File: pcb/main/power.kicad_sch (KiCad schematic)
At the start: 13 parts, among them U1 LXDC55FAAA-203, U2 LT1963AES3-3.3

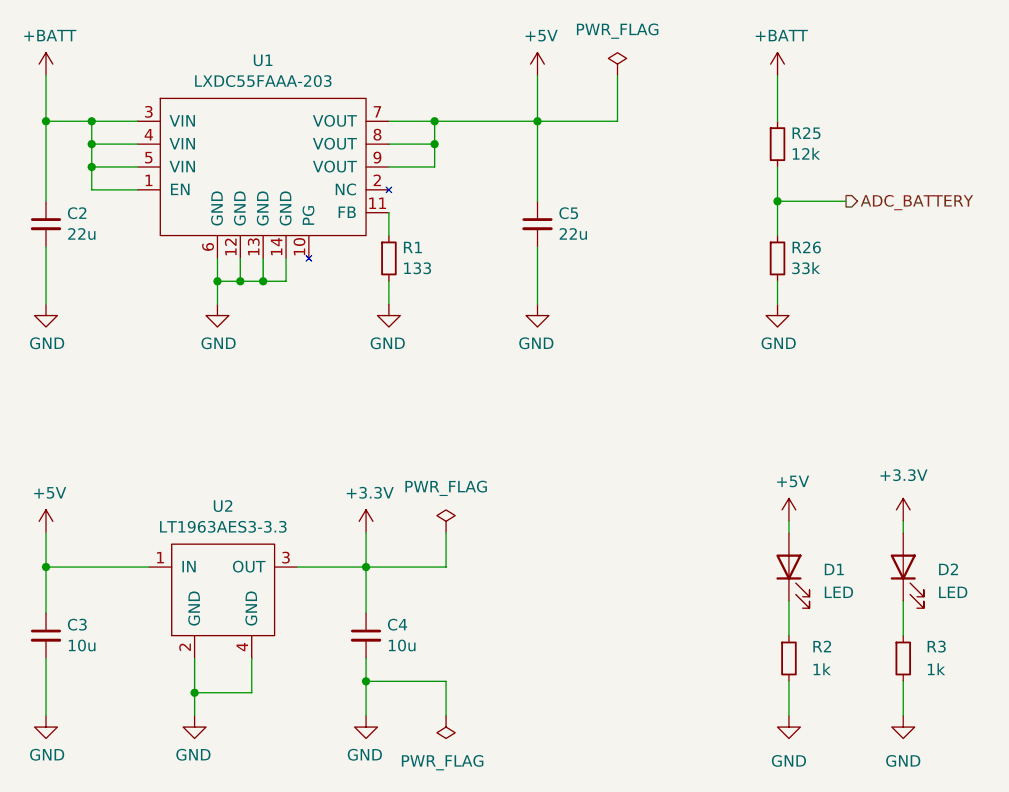
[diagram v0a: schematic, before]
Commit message: feat: delete two CAN connectors & add microSD input pin
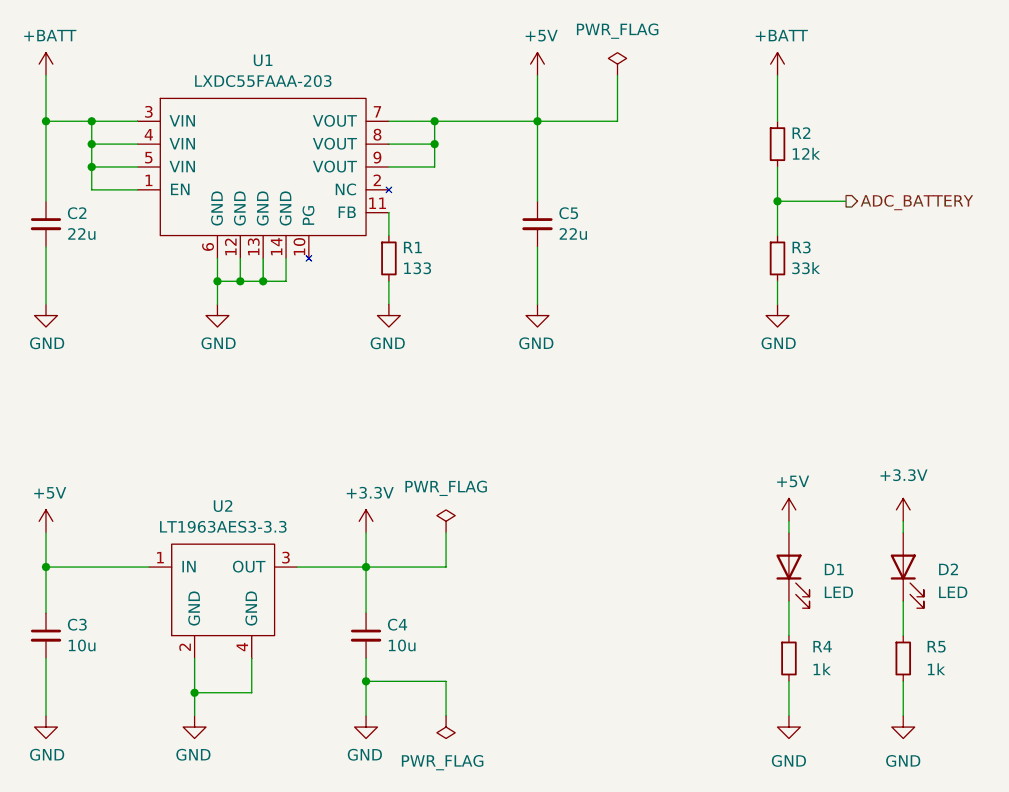
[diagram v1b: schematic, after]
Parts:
- renumbered R25 to R2, R26 to R3, R2 to R4, R3 to R5
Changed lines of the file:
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@@
 		(on_board yes)
 		(dnp no)
-		(property "Reference" "#PWR034"
+		(property "Reference" "#PWR032"
 			(at 184.15 104.14 0)
 			(effects
@@
 			(project "main"
 				(path "/656d7f7e-2105-4d24-8d0a-93f423922a26/b1cff48c-95d9-4c57-9a68-4399c567f645"
-					(reference "#PWR034")
+					(reference "#PWR032")
 					(unit 1)
 				)
@@
 		(on_board yes)
 		(dnp no)
-		(property "Reference" "#PWR024"
+		(property "Reference" "#PWR020"
 			(at 101.6 82.55 0)
 			(effects
@@
 			(project ""
 				(path "/656d7f7e-2105-4d24-8d0a-93f423922a26/b1cff48c-95d9-4c57-9a68-4399c567f645"
-					(reference "#PWR024")
+					(reference "#PWR020")
 					(unit 1)
 				)
@@
 		(on_board yes)
 		(dnp no)
-		(property "Reference" "#PWR025"
+		(property "Reference" "#PWR021"
 			(at 101.6 105.41 0)
 			(effects
@@
 			(project "main"
 				(path "/656d7f7e-2105-4d24-8d0a-93f423922a26/b1cff48c-95d9-4c57-9a68-4399c567f645"
-					(reference "#PWR025")
+					(reference "#PWR021")
 					(unit 1)
 				)
@@
 		(dnp no)
 		(fields_autoplaced yes)
-		(property "Reference" "R2"
+		(property "Reference" "R4"
 			(at 186.69 114.2999 0)
 			(effects
@@
 			(project "main"
 				(path "/656d7f7e-2105-4d24-8d0a-93f423922a26/b1cff48c-95d9-4c57-9a68-4399c567f645"
-					(reference "R2")
+					(reference "R4")
 					(unit 1)
 				)
@@
 		(on_board yes)
 		(dnp no)
-		(property "Reference" "#PWR074"
+		(property "Reference" "#PWR030"
 			(at 182.88 54.61 0)
 			(effects
@@
 			(project "main"
 				(path "/656d7f7e-2105-4d24-8d0a-93f423922a26/b1cff48c-95d9-4c57-9a68-4399c567f645"
-					(reference "#PWR074")
+					(reference "#PWR030")
 					(unit 1)
 				)
@@
 		(dnp no)
 		(fields_autoplaced yes)
-		(property "Reference" "#PWR037"
+		(property "Reference" "#PWR035"
 			(at 196.85 128.27 0)
 			(effects
@@
 			(project ""
 				(path "/656d7f7e-2105-4d24-8d0a-93f423922a26/b1cff48c-95d9-4c57-9a68-4399c567f645"
-					(reference "#PWR037")
+					(reference "#PWR035")
 					(unit 1)
 				)
@@
 		(on_board yes)
 		(dnp no)
-		(property "Reference" "R25"
+		(property "Reference" "R2"
 			(at 184.3786 57.2516 0)
 			(effects
@@
 			(project "main"
 				(path "/656d7f7e-2105-4d24-8d0a-93f423922a26/b1cff48c-95d9-4c57-9a68-4399c567f645"
-					(reference "R25")
+					(reference "R2")
 					(unit 1)
 				)
@@
 		(on_board yes)
 		(dnp no)
-		(property "Reference" "#PWR026"
+		(property "Reference" "#PWR022"
 			(at 101.6 128.27 0)
 			(effects
@@
 			(project "main"
 				(path "/656d7f7e-2105-4d24-8d0a-93f423922a26/b1cff48c-95d9-4c57-9a68-4399c567f645"
-					(reference "#PWR026")
+					(reference "#PWR022")
 					(unit 1)
 				)
@@
 		(dnp no)
 		(fields_autoplaced yes)
-		(property "Reference" "#PWR035"
+		(property "Reference" "#PWR033"
 			(at 184.15 128.27 0)
 			(effects
@@
 			(project "main"
 				(path "/656d7f7e-2105-4d24-8d0a-93f423922a26/b1cff48c-95d9-4c57-9a68-4399c567f645"
-					(reference "#PWR035")
+					(reference "#PWR033")
 					(unit 1)
 				)
@@
 		(on_board yes)
 		(dnp no)
-		(property "Reference" "#PWR073"
+		(property "Reference" "#PWR031"
 			(at 182.88 82.55 0)
 			(effects
@@
 			(project "main"
 				(path "/656d7f7e-2105-4d24-8d0a-93f423922a26/b1cff48c-95d9-4c57-9a68-4399c567f645"
-					(reference "#PWR073")
+					(reference "#PWR031")
 					(unit 1)
 				)
@@
 		(on_board yes)
 		(dnp no)
-		(property "Reference" "#PWR028"
+		(property "Reference" "#PWR024"
 			(at 120.65 82.55 0)
 			(effects
@@
 			(project ""
 				(path "/656d7f7e-2105-4d24-8d0a-93f423922a26/b1cff48c-95d9-4c57-9a68-4399c567f645"
-					(reference "#PWR028")
+					(reference "#PWR024")
 					(unit 1)
 				)
@@
 		(on_board yes)
 		(dnp no)
-		(property "Reference" "#PWR030"
+		(property "Reference" "#PWR026"
 			(at 137.16 128.27 0)
 			(effects
@@
 			(project "main"
 				(path "/656d7f7e-2105-4d24-8d0a-93f423922a26/b1cff48c-95d9-4c57-9a68-4399c567f645"
-					(reference "#PWR030")
+					(reference "#PWR026")
 					(unit 1)
 				)
@@
 		(dnp no)
 		(fields_autoplaced yes)
-		(property "Reference" "#PWR036"
+		(property "Reference" "#PWR034"
 			(at 196.85 104.14 0)
 			(effects
@@
 			(project ""
 				(path "/656d7f7e-2105-4d24-8d0a-93f423922a26/b1cff48c-95d9-4c57-9a68-4399c567f645"
-					(reference "#PWR036")
+					(reference "#PWR034")
 					(unit 1)
 				)
@@
 		(on_board yes)
 		(dnp no)
-		(property "Reference" "#PWR032"
+		(property "Reference" "#PWR028"
 			(at 156.21 54.61 0)
 			(effects
@@
 			(project ""
 				(path "/656d7f7e-2105-4d24-8d0a-93f423922a26/b1cff48c-95d9-4c57-9a68-4399c567f645"
-					(reference "#PWR032")
+					(reference "#PWR028")
 					(unit 1)
 				)
@@
 		(on_board yes)
 		(dnp no)
-		(property "Reference" "#PWR033"
+		(property "Reference" "#PWR029"
 			(at 156.21 82.55 0)
 			(effects
@@
 			(project ""
 				(path "/656d7f7e-2105-4d24-8d0a-93f423922a26/b1cff48c-95d9-4c57-9a68-4399c567f645"
-					(reference "#PWR033")
+					(reference "#PWR029")
 					(unit 1)
 				)
@@
 		(on_board yes)
 		(dnp no)
-		(property "Reference" "#PWR031"
+		(property "Reference" "#PWR027"
 			(at 139.7 82.55 0)
 			(effects
@@
 			(project ""
 				(path "/656d7f7e-2105-4d24-8d0a-93f423922a26/b1cff48c-95d9-4c57-9a68-4399c567f645"
-					(reference "#PWR031")
+					(reference "#PWR027")
 					(unit 1)
 				)
@@
 		(dnp no)
 		(fields_autoplaced yes)
-		(property "Reference" "R3"
+		(property "Reference" "R5"
 			(at 199.39 114.2999 0)
 			(effects
@@
 			(project ""
 				(path "/656d7f7e-2105-4d24-8d0a-93f423922a26/b1cff48c-95d9-4c57-9a68-4399c567f645"
-					(reference "R3")
+					(reference "R5")
 					(unit 1)
 				)
@@
 		(on_board yes)
 		(dnp no)
-		(property "Reference" "R26"
+		(property "Reference" "R3"
 			(at 184.3786 69.9516 0)
 			(effects
@@
 			(project "main"
 				(path "/656d7f7e-2105-4d24-8d0a-93f423922a26/b1cff48c-95d9-4c57-9a68-4399c567f645"
-					(reference "R26")
+					(reference "R3")
 					(unit 1)
 				)
@@
 		(on_board yes)
 		(dnp no)
-		(property "Reference" "#PWR027"
+		(property "Reference" "#PWR023"
 			(at 118.11 128.27 0)
 			(effects
@@
 			(project "main"
 				(path "/656d7f7e-2105-4d24-8d0a-93f423922a26/b1cff48c-95d9-4c57-9a68-4399c567f645"
-					(reference "#PWR027")
+					(reference "#PWR023")
 					(unit 1)
 				)
@@
 		(on_board yes)
 		(dnp no)
-		(property "Reference" "#PWR029"
+		(property "Reference" "#PWR025"
 			(at 137.16 105.41 0)
 			(effects
@@
 			(project "main"
 				(path "/656d7f7e-2105-4d24-8d0a-93f423922a26/b1cff48c-95d9-4c57-9a68-4399c567f645"
-					(reference "#PWR029")
+					(reference "#PWR025")
 					(unit 1)
 				)
@@
 		(on_board yes)
 		(dnp no)
-		(property "Reference" "#PWR023"
+		(property "Reference" "#PWR019"
 			(at 101.6 54.61 0)
 			(effects
@@
 			(project ""
 				(path "/656d7f7e-2105-4d24-8d0a-93f423922a26/b1cff48c-95d9-4c57-9a68-4399c567f645"
-					(reference "#PWR023")
-					(unit 1)
-				)
+					(reference "#PWR019")
+					(unit 1)
+				)
